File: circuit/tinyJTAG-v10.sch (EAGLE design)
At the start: 16 parts, among them IC1 TINY85S, IC2 74125SOIC14, Q2 MMBT3906LT1SMD, X1 USBPCB

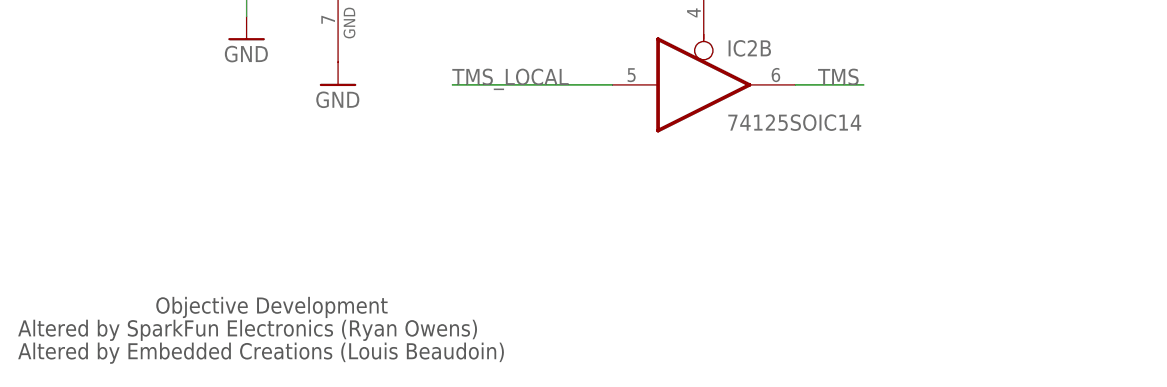
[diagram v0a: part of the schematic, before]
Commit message: added CC info back
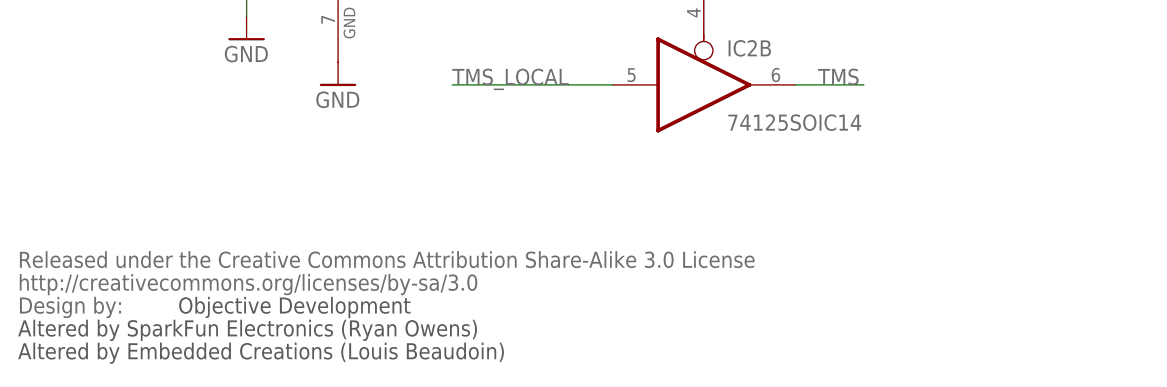
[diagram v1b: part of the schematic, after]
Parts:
- added U$4: CREATIVE_COMMONS, SparkFun:CREATIVE_COMMONS
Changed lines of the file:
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@@
 <layer number="223" name="223bmp" color="24" fill="1" visible="no" active="no"/>
 <layer number="224" name="224bmp" color="25" fill="1" visible="no" active="no"/>
+<layer number="250" name="Descript" color="3" fill="1" visible="no" active="no"/>
 <layer number="251" name="SMDround" color="12" fill="11" visible="no" active="no"/>
 <layer number="254" name="cooling" color="7" fill="1" visible="yes" active="yes"/>
@@
 <part name="R5" library="SparkFun" deviceset="RESISTOR" device="0603-RES"/>
 <part name="C2" library="rcl" deviceset="C-EU" device="C0805" value="10uF"/>
+<part name="U$4" library="SparkFun" deviceset="CREATIVE_COMMONS" device=""/>
 </parts>
 <sheets>
 <sheet>
 <plain>
-<text x="17.78" y="7.62" size="1.778" layer="97">Objective Development</text>
+<text x="20.32" y="7.62" size="1.778" layer="97">Objective Development</text>
 <text x="2.54" y="5.08" size="1.778" layer="97">Altered by SparkFun Electronics (Ryan Owens)</text>
 <text x="2.54" y="2.54" size="1.778" layer="97">Altered by Embedded Creations (Louis Beaudoin)</text>
@@
 <instance part="R5" gate="G$1" x="134.62" y="53.34" rot="R180"/>
 <instance part="C2" gate="G$1" x="233.68" y="167.64"/>
+<instance part="U$4" gate="G$1" x="2.54" y="7.62"/>
 </instances>
 <busses>

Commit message: added "draft" to title
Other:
- note added: "(Draft)"
- moved on the sheet: D3, D4, IC1, R1, R2, R3, U$5

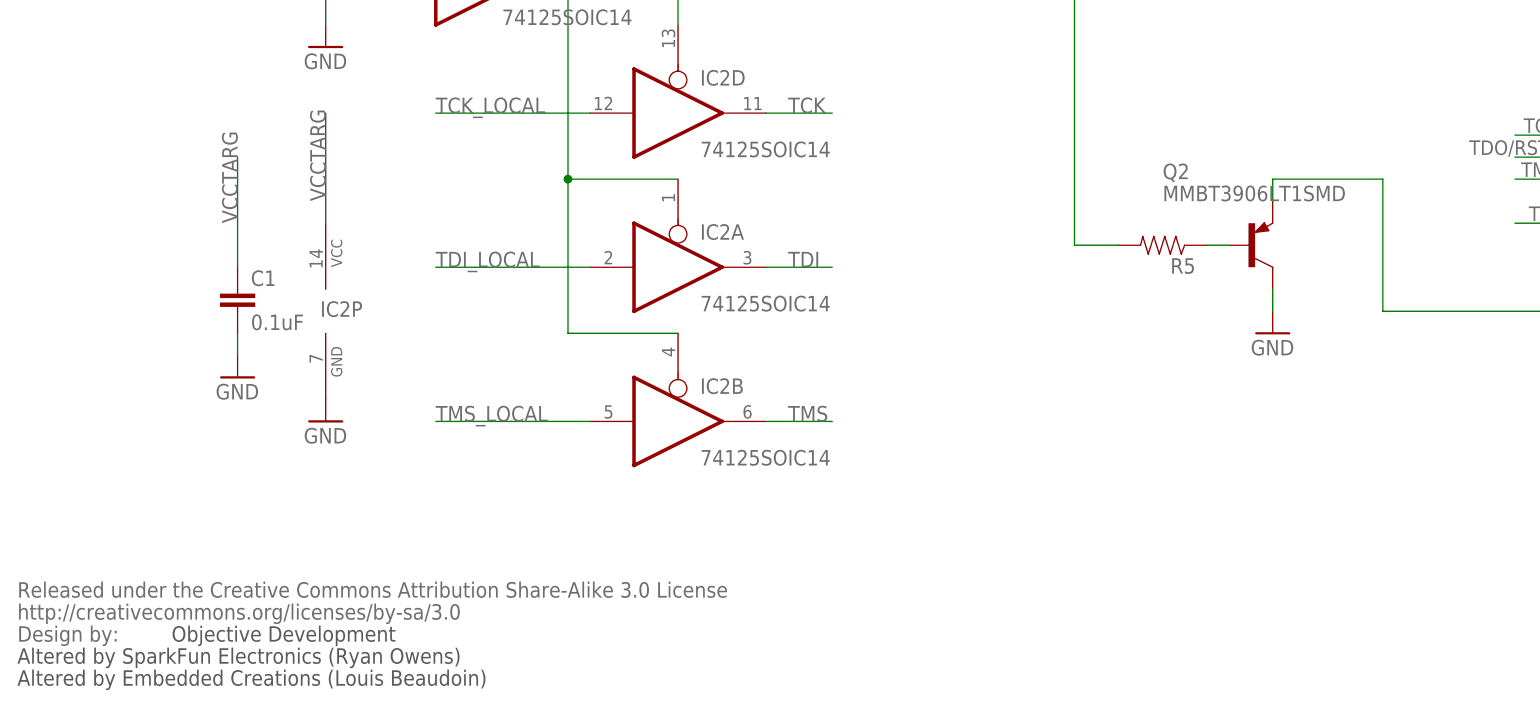
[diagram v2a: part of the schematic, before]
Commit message: Version sent for manufacturing initial prototypes
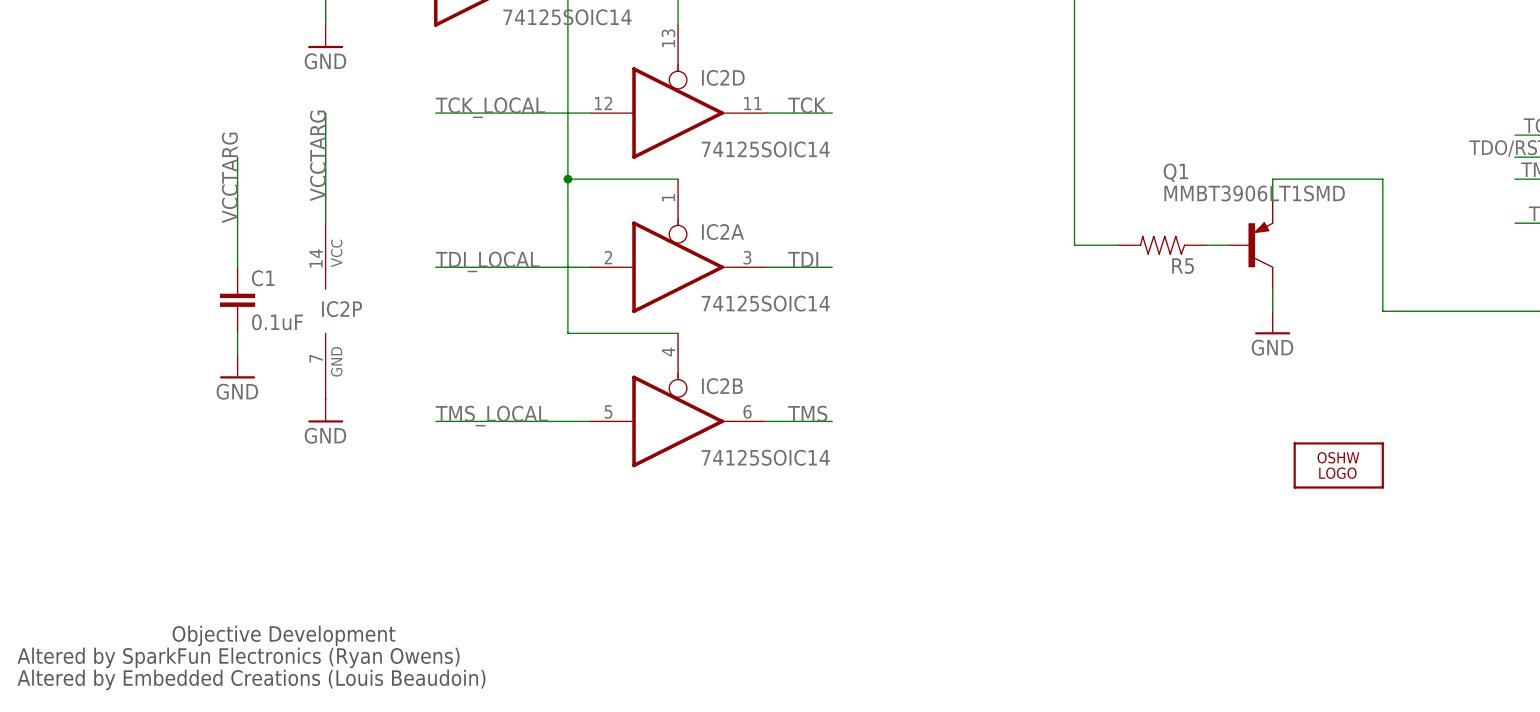
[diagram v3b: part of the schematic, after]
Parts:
- removed U$4: CREATIVE_COMMONS, SparkFun:CREATIVE_COMMONS
- added LOGO1: OSHW_LOGO_FILLX0150-NT, ohw-logo:OSHW_LOGO_FILLX0150-NT
- renumbered Q2 to Q1
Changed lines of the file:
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@@
 <?xml version="1.0" encoding="utf-8"?>
 <!DOCTYPE eagle SYSTEM "eagle.dtd">
-<eagle version="6.1">
+<eagle version="6.2">
 <drawing>
 <settings>
@@
 <part name="C1" library="SparkFun" deviceset="CAP" device="0603-CAP" value="0.1uF"/>
 <part name="GND11" library="supply1" deviceset="GND" device=""/>
-<part name="Q2" library="transistor-pnp" deviceset="MMBT3906*" device="SMD" technology="LT1"/>
+<part name="Q1" library="transistor-pnp" deviceset="MMBT3906*" device="SMD" technology="LT1"/>
 <part name="R5" library="SparkFun" deviceset="RESISTOR" device="0603-RES"/>
 <part name="C2" library="rcl" deviceset="C-EU" device="C0805" value="10uF"/>
-<part name="U$4" library="SparkFun" deviceset="CREATIVE_COMMONS" device=""/>
+<part name="LOGO1" library="ohw-logo" deviceset="OSHW_LOGO_FILL" device="X0150-NT"/>
 </parts>
 <sheets>
@@
 <instance part="C1" gate="G$1" x="27.94" y="45.72"/>
 <instance part="GND11" gate="1" x="147.32" y="43.18"/>
-<instance part="Q2" gate="G$1" x="144.78" y="53.34"/>
+<instance part="Q1" gate="G$1" x="144.78" y="53.34"/>
 <instance part="R5" gate="G$1" x="134.62" y="53.34" rot="R180"/>
 <instance part="C2" gate="G$1" x="233.68" y="167.64"/>
-<instance part="U$4" gate="G$1" x="2.54" y="7.62"/>
+<instance part="LOGO1" gate="G$1" x="154.94" y="27.94"/>
 </instances>
 <busses>
@@
 <wire x1="147.32" y1="45.72" x2="147.32" y2="48.26" width="0.1524" layer="91"/>
 <pinref part="GND11" gate="1" pin="GND"/>
-<pinref part="Q2" gate="G$1" pin="C"/>
+<pinref part="Q1" gate="G$1" pin="C"/>
 </segment>
 </net>
@@
 <wire x1="160.02" y1="60.96" x2="147.32" y2="60.96" width="0.1524" layer="91"/>
 <wire x1="147.32" y1="60.96" x2="147.32" y2="58.42" width="0.1524" layer="91"/>
-<pinref part="Q2" gate="G$1" pin="E"/>
+<pinref part="Q1" gate="G$1" pin="E"/>
 </segment>
 </net>
 <net name="N$4" class="0">
 <segment>
-<pinref part="Q2" gate="G$1" pin="B"/>
+<pinref part="Q1" gate="G$1" pin="B"/>
 <pinref part="R5" gate="G$1" pin="1"/>
 <wire x1="142.24" y1="53.34" x2="139.7" y2="53.34" width="0.1524" layer="91"/>
@@
 </sheet>
 </sheets>
-<errors>
-</errors>
 </schematic>
 </drawing>
